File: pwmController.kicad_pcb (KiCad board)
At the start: 2 copper layers, 100 x 70 mm, 48 parts, among them J1 RJ12, J14 inputs, J16 relays, J17 relays, J5 power, J6 gnd, J7 inputs, J8 track out, K1 G5V-1, K2 G5V-1, K3 G5V-1, K4 G5V-1, K5 G5V-1, K6 G5V-1, K7 G5V-1, K8 G5V-1, U1 24LC256, U2 MAX485E, U3 L298N, U4 MCP23017_SP, U5 ULN2803A, U6 PCF8574, U7 Buck

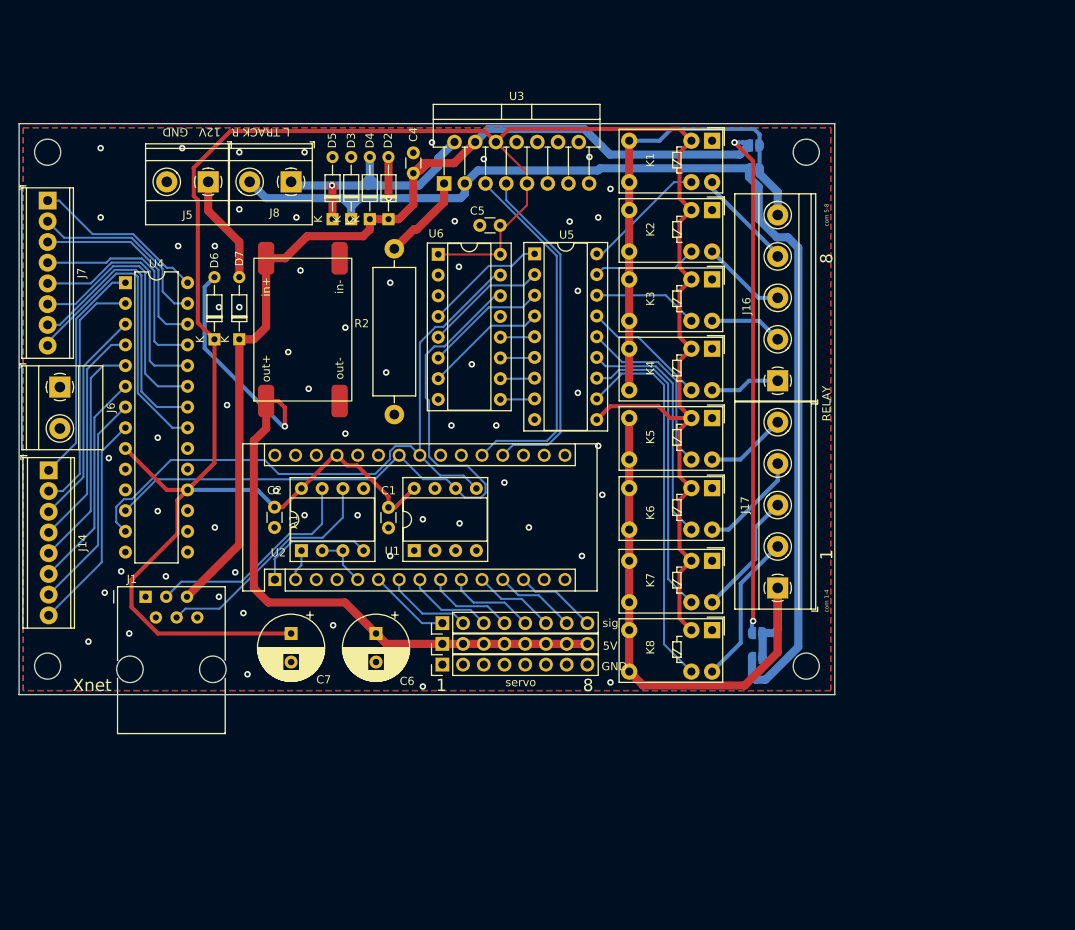
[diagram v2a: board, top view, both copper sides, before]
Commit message: made drastic changes to PCB design. I added 2nd Rj12 connector, side by side connectors, 2 analog inpouts and 2nd channel of H bridge is commissioned
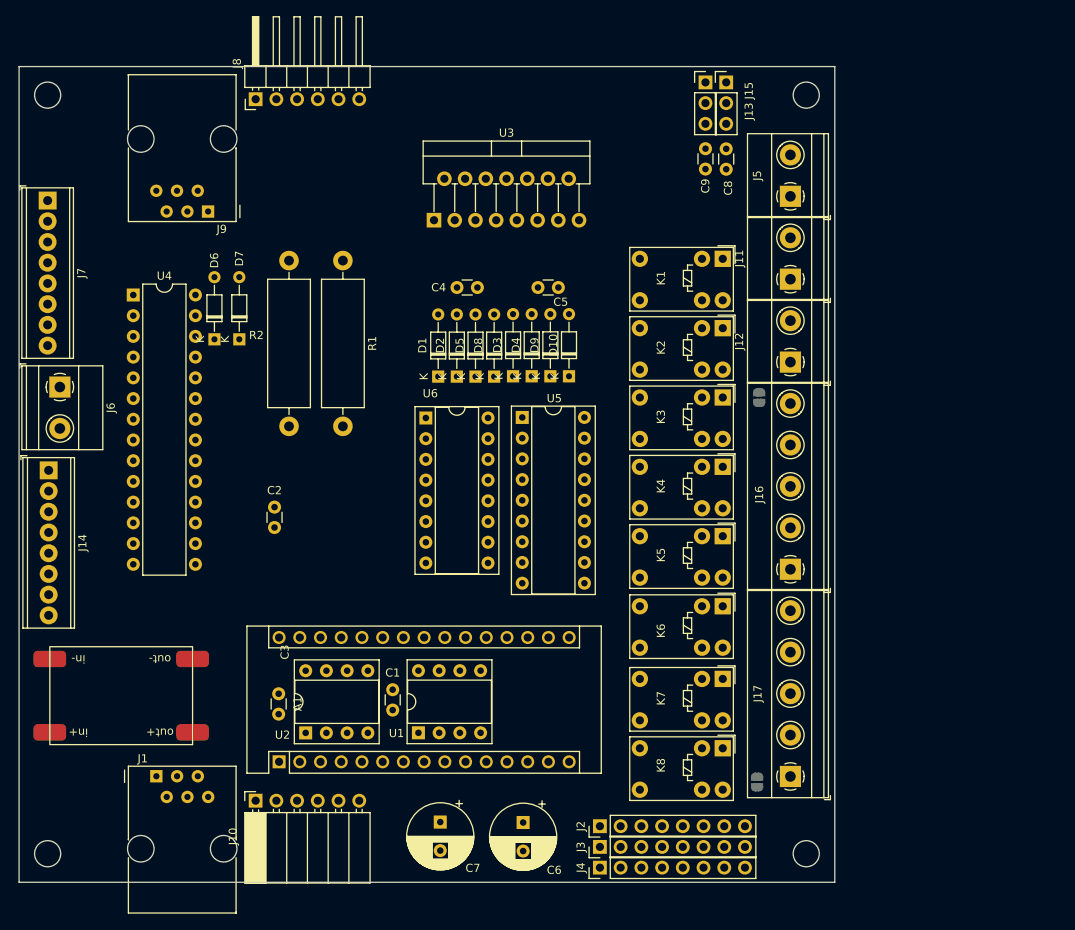
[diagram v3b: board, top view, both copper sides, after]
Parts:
- removed 5V, GND, sig: Conn_01x08_Male, Connector_PinHeader_2.54mm:PinHeader_1x08_P2.54mm_Vertical
- removed JP2, JP4: jmp, Jumper:SolderJumper-2_P1.3mm_Open_RoundedPad1.0x1.5mm
- removed the REF** at (71.5, 99.5)
- removed the REF** at (164.5, 99.5)
- removed the REF** at (164.5, 36.5)
- removed the REF** at (71.5, 36.5)
- added C3: 100nF, Capacitor_THT:C_Disc_D3.0mm_W1.6mm_P2.50mm, F.Cu at (99.8, 102.9)
- added C8: 100nF, Capacitor_THT:C_Disc_D3.0mm_W1.6mm_P2.50mm, F.Cu at (154.7, 38.6)
- added C9: 100nF, Capacitor_THT:C_Disc_D3.0mm_W1.6mm_P2.50mm, F.Cu at (152.1, 38.6)
- added D1: D, Diode_THT:D_DO-34_SOD68_P7.62mm_Horizontal, F.Cu at (119.4, 64.0)
- added D10: D, Diode_THT:D_DO-34_SOD68_P7.62mm_Horizontal, F.Cu at (135.4, 64.0)
- added D8: D, Diode_THT:D_DO-34_SOD68_P7.62mm_Horizontal, F.Cu at (126.2, 64.0)
- added D9: D, Diode_THT:D_DO-34_SOD68_P7.62mm_Horizontal, F.Cu at (133.1, 64.0)
- added J10: Conn_01x06_Female, Connector_PinSocket_2.54mm:PinSocket_1x06_P2.54mm_Horizontal, F.Cu at (97.0, 116.0)
- added J11: track out, TerminalBlock_Phoenix:TerminalBlock_Phoenix_MKDS-1,5-2-5.08_1x02_P5.08mm_Horizontal, F.Cu at (162.6, 52.1)
- added J12: track out, TerminalBlock_Phoenix:TerminalBlock_Phoenix_MKDS-1,5-2-5.08_1x02_P5.08mm_Horizontal, F.Cu at (162.6, 62.2)
- added J13: ADC, Connector_PinHeader_2.54mm:PinHeader_1x03_P2.54mm_Vertical, F.Cu at (152.1, 27.9)
- added J15: ADC, Connector_PinHeader_2.54mm:PinHeader_1x03_P2.54mm_Vertical, F.Cu at (154.7, 27.9)
- added J2: Conn_01x08_Male, Connector_PinHeader_2.54mm:PinHeader_1x08_P2.54mm_Vertical, F.Cu at (139.2, 119.1)
- added J3: Conn_01x08_Male, Connector_PinHeader_2.54mm:PinHeader_1x08_P2.54mm_Vertical, F.Cu at (139.2, 121.7)
- added J4: Conn_01x08_Male, Connector_PinHeader_2.54mm:PinHeader_1x08_P2.54mm_Vertical, F.Cu at (139.2, 124.2)
- added J9: RJ12, Connector_RJ:RJ12_Amphenol_54601, F.Cu at (91.2, 43.8)
- added R1: R, Resistor_THT:R_Axial_DIN0516_L15.5mm_D5.0mm_P20.32mm_Horizontal, F.Cu at (107.7, 49.8)
- added REF**: MountingHole_3.2mm_M3, MountingHole:MountingHole_3.2mm_M3, F.Cu at (164.5, 29.5)
- added REF**: MountingHole_3.2mm_M3, MountingHole:MountingHole_3.2mm_M3, F.Cu at (164.5, 122.5)
- added REF**: MountingHole_3.2mm_M3, MountingHole:MountingHole_3.2mm_M3, F.Cu at (71.5, 122.5)
- added REF**: MountingHole_3.2mm_M3, MountingHole:MountingHole_3.2mm_M3, F.Cu at (71.5, 29.5)
- J8: value track out -> Conn_01x06_Male; footprint TerminalBlock_Phoenix:TerminalBlock_Phoenix_MKDS-1,5-2-5.08_1x02_P5.08mm_Horizontal -> Connector_PinHeader_2.54mm:PinHeader_1x06_P2.54mm_Horizontal
- moved J5 71.4 mm to (162.6, 41.9), turned to 90 degrees
- moved U7 47.9 mm to (82.8, 104.6), turned to 180 degrees
- moved JP1 30.9 mm to (158.7, 66.6), turned to -90 degrees
- moved C7 29.5 mm to (119.6, 118.6)
- moved C6 29.4 mm to (129.8, 118.7)
- moved D3 27.7 mm to (128.6, 64.0)
- moved D4 27.7 mm to (130.8, 64.0)
- moved D5 26.1 mm to (124.0, 64.0)
- moved J17 23.2 mm to (162.6, 113.0)
- moved J16 23.2 mm to (162.6, 87.6)
- moved U2 22.3 mm to (103.1, 107.7)
- moved A1 22.3 mm to (99.9, 111.2)
- moved C1 22.3 mm to (113.8, 102.4)
- moved U1 22.3 mm to (117.0, 107.7)
- moved J1 22.0 mm to (84.8, 113.0)
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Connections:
- net /coil5_ renamed Net-(U6-Pad7)
- net /coil6_ renamed Net-(U6-Pad6)
- net /coil7_ renamed Net-(U6-Pad5)
- net /coil8_ renamed Net-(U6-Pad4)
- A1 pad 12: servo7 -> pwm2
- A1 pad 13: servo8 -> pwm1
- A1 pad 14: unconnected-(A1-Pad14) -> pwm3
- A1 pad 15: unconnected-(A1-Pad15) -> pwm4
- A1 pad 19: pwm1 -> servo7
- A1 pad 20: pwm2 -> servo8
- A1 pad 21: overcurrent -> ADC1
- A1 pad 22: unconnected-(A1-Pad22) -> ADC2
- A1 pad 25: unconnected-(A1-Pad25) -> CS1
- A1 pad 26: unconnected-(A1-Pad26) -> CS2
- D2 pad 1: +12V -> track1R
- D2 pad 2: /rightTrack -> GND
- D3 pad 1: /rightTrack -> +12V
- D3 pad 2: GND -> track2R
- D4 pad 1: +12V -> track2R
- D4 pad 2: Net-(D4-Pad2) -> GND
- D5 pad 1: Net-(D4-Pad2) -> +12V
- D5 pad 2: GND -> track1L
- D7 pad 1: +12V -> Net-(U7-Pad4)
- J1 pad 3: Net-(J1-Pad3) -> /B
- J1 pad 4: Net-(J1-Pad4) -> /A
- J8 pad 1: Net-(D4-Pad2) -> GND
- J8 pad 2: /rightTrack -> GND
- R2 pad 1: Net-(R2-Pad1) -> GND
- R2 pad 2: GND -> CS1
- U2 pad 6: Net-(J1-Pad4) -> /A
- U2 pad 7: Net-(J1-Pad3) -> /B
- U3 pad 1: Net-(R2-Pad1) -> CS1
- U3 pad 10: unconnected-(U3-Pad10) -> pwm4
- U3 pad 11: unconnected-(U3-Pad11) -> +5V
- U3 pad 12: unconnected-(U3-Pad12) -> pwm3
- U3 pad 13: unconnected-(U3-Pad13) -> track2R
- U3 pad 14: unconnected-(U3-Pad14) -> track2L
- U3 pad 15: unconnected-(U3-Pad15) -> CS2
- U3 pad 2: Net-(D4-Pad2) -> track1R
- U3 pad 3: /rightTrack -> track1L
- U5 pad 5: /coil4_ -> Net-(U6-Pad9)
- U5 pad 6: /coil3_ -> Net-(U6-Pad10)
- U5 pad 7: /coil2_ -> Net-(U6-Pad11)
- U5 pad 8: /coil1_ -> Net-(U6-Pad12)
- U6 pad 10: /coil2_ -> Net-(U6-Pad10)
- U6 pad 11: /coil3_ -> Net-(U6-Pad11)
- U6 pad 12: /coil4_ -> Net-(U6-Pad12)
- U6 pad 9: /coil1_ -> Net-(U6-Pad9)
- U7 pad 4: +12V -> Net-(U7-Pad4)
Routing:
- net +5V: track 296.2 -> 0.00 mm
- net +12V: track 183.0 -> 0.00 mm, vias 2 -> 0
- net /rightTrack: track 146.5 -> 0.00 mm, vias 1 -> 0
- net +5VA: track 95.2 -> 0.00 mm, vias 1 -> 0
- net SCL: track 83.5 -> 0.00 mm
- net SDA: track 81.9 -> 0.00 mm
- net Net-(J17-Pad1): track 69.8 -> 0.00 mm
- net Net-(J16-Pad5): track 58.2 -> 0.00 mm
- net /coil8: track 46.8 -> 0.00 mm
- net pwm2: track 44.4 -> 0.00 mm
- net pwm1: track 41.5 -> 0.00 mm
- net /coil7: track 37.8 -> 0.00 mm
- net Net-(J7-Pad8): track 37.3 -> 0.00 mm
- net Net-(J7-Pad7): track 35.3 -> 0.00 mm
- net Net-(D4-Pad2): track 33.7 -> 0.00 mm, vias 1 -> 0
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- removed copper zone on B.Cu, net GND
- removed copper zone on F.Cu, net GND
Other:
- board size 100 x 70 mm -> 100 x 100 mm
- board text removed: "1"
- board text removed: "12V"
- board text removed: "8"
- board text removed: "L TRACK R 12V GND"
- board text removed: "RELAY"
- board text removed: "Xnet"
- board text removed: "Xnet PWM controller And IO module V1.0 By Bas Knippels"
- board text removed: "com 1-4"
- board text removed: "com 5-8"
- board text removed: "servo"
- board text removed: "track right"

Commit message: divided the schematic in several sheets.
PCB needs to be redrawn because the link between components is gone
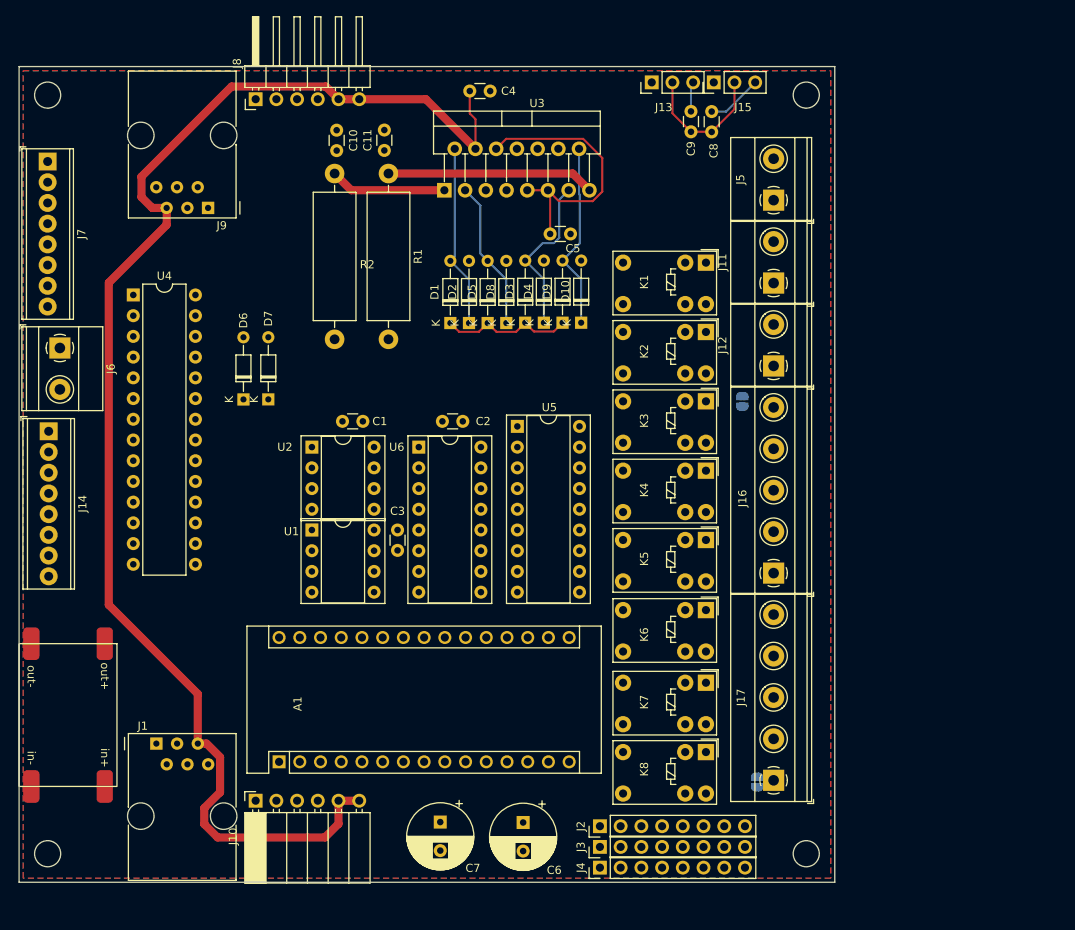
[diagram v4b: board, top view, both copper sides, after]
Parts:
- added C10: 100nF, Capacitor_THT:C_Disc_D3.0mm_W1.6mm_P2.50mm, F.Cu at (106.9, 33.8)
- added C11: 100nF, Capacitor_THT:C_Disc_D3.0mm_W1.6mm_P2.50mm, F.Cu at (112.8, 36.3)
- moved U2 35.0 mm to (103.9, 72.7), turned to 0 degrees
- moved C1 33.1 mm to (110.1, 69.5), turned to 180 degrees
- moved U1 28.1 mm to (103.9, 82.8), turned to 0 degrees
- moved C2 25.4 mm to (122.4, 69.5), turned to 180 degrees
- moved C3 24.8 mm to (114.4, 82.8)
- moved C4 24.1 mm to (123.2, 29.0), turned to 0 degrees
- moved R1 12.0 mm to (113.3, 39.1)
- moved R2 11.2 mm to (106.7, 59.4), turned to 90 degrees
- moved D7 8.18 mm to (98.6, 66.8)
- moved D6 8.18 mm to (95.5, 66.8)
- moved U7 7.40 mm to (75.5, 103.2), turned to -90 degrees
- moved C5 6.73 mm to (133.1, 46.5)
- moved D1 6.73 mm to (120.9, 57.4)
- moved D10 6.73 mm to (136.9, 57.4)
- moved D2 6.73 mm to (123.2, 57.4)
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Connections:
- U5 pad 5: Net-(U6-Pad9) -> Net-(U5-Pad5)
- U5 pad 6: Net-(U6-Pad10) -> Net-(U5-Pad6)
- U5 pad 7: Net-(U6-Pad11) -> Net-(U5-Pad7)
- U5 pad 8: Net-(U6-Pad12) -> Net-(U5-Pad8)
- U6 pad 10: Net-(U6-Pad10) -> Net-(U5-Pad7)
- U6 pad 11: Net-(U6-Pad11) -> Net-(U5-Pad6)
- U6 pad 12: Net-(U6-Pad12) -> Net-(U5-Pad5)
- U6 pad 9: Net-(U6-Pad9) -> Net-(U5-Pad8)
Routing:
- net +12V: track 0.00 -> 187.4 mm
- net +5V: track 0.00 -> 51.1 mm
- net CS2: track 0.00 -> 25.5 mm
- net track2L: track 0.00 -> 23.2 mm
- net track1R: track 0.00 -> 22.5 mm
- net track2R: track 0.00 -> 20.2 mm
- net track1L: track 0.00 -> 18.4 mm
- net CS1: track 0.00 -> 14.3 mm
- net ADC1: track 0.00 -> 6.82 mm
- net ADC2: track 0.00 -> 3.67 mm
- added copper zone on B.Cu, net GND
- added copper zone on F.Cu, net GND

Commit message: changed PCB layout. I want to change more
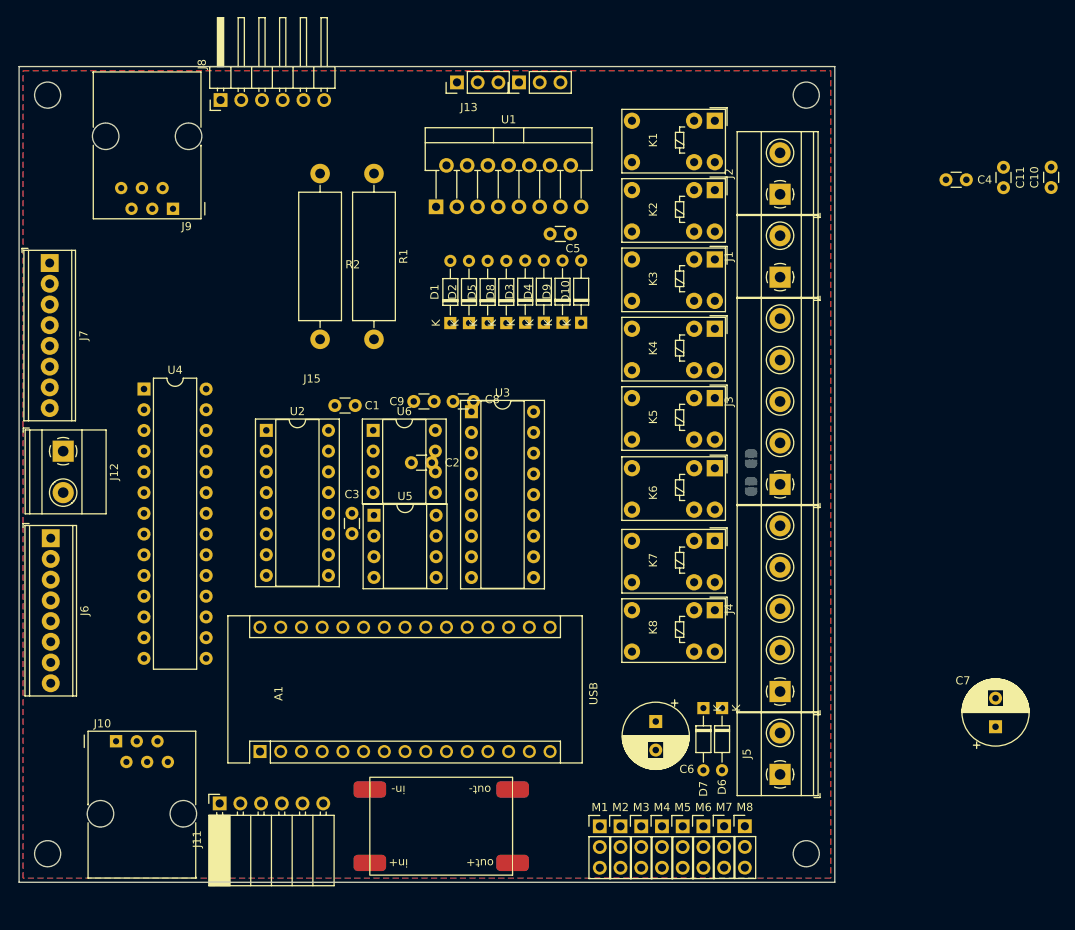
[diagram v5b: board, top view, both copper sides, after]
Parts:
- removed J14: inputs, TerminalBlock_Phoenix:TerminalBlock_Phoenix_MPT-0,5-8-2.54_1x08_P2.54mm_Horizontal
- removed J16, J17: relays, TerminalBlock_Phoenix:TerminalBlock_Phoenix_MKDS-1,5-5-5.08_1x05_P5.08mm_Horizontal
- removed JP3: jmp, Jumper:SolderJumper-2_P1.3mm_Open_RoundedPad1.0x1.5mm
- added JP2: jmp, Jumper:SolderJumper-2_P1.3mm_Open_RoundedPad1.0x1.5mm, B.Cu at (157.7, 77.5)
- added M1: Motor_Servo, Connector_PinHeader_2.54mm:PinHeader_1x03_P2.54mm_Vertical, F.Cu at (139.2, 119.1)
- added M2: Motor_Servo, Connector_PinHeader_2.54mm:PinHeader_1x03_P2.54mm_Vertical, F.Cu at (141.7, 119.1)
- added M3: Motor_Servo, Connector_PinHeader_2.54mm:PinHeader_1x03_P2.54mm_Vertical, F.Cu at (144.3, 119.1)
- added M4: Motor_Servo, Connector_PinHeader_2.54mm:PinHeader_1x03_P2.54mm_Vertical, F.Cu at (146.8, 119.1)
- added M5: Motor_Servo, Connector_PinHeader_2.54mm:PinHeader_1x03_P2.54mm_Vertical, F.Cu at (149.4, 119.1)
- added M6: Motor_Servo, Connector_PinHeader_2.54mm:PinHeader_1x03_P2.54mm_Vertical, F.Cu at (151.9, 119.1)
- added M7: Motor_Servo, Connector_PinHeader_2.54mm:PinHeader_1x03_P2.54mm_Vertical, F.Cu at (154.4, 119.1)
- added M8: Motor_Servo, Connector_PinHeader_2.54mm:PinHeader_1x03_P2.54mm_Vertical, F.Cu at (157.0, 119.1)
- J1: value RJ12 -> track out; footprint Connector_RJ:RJ12_Amphenol_54601 -> TerminalBlock_Phoenix:TerminalBlock_Phoenix_MKDS-1,5-2-5.08_1x02_P5.08mm_Horizontal
- J10: value Conn_01x06_Female -> RJ12; footprint Connector_PinSocket_2.54mm:PinSocket_1x06_P2.54mm_Horizontal -> Connector_RJ:RJ12_Amphenol_54601
- J11: value track out -> Conn_01x06_Female; footprint TerminalBlock_Phoenix:TerminalBlock_Phoenix_MKDS-1,5-2-5.08_1x02_P5.08mm_Horizontal -> Connector_PinSocket_2.54mm:PinSocket_1x06_P2.54mm_Horizontal
- J12: value track out -> gnd
- J2: value Conn_01x08_Male -> track out; footprint Connector_PinHeader_2.54mm:PinHeader_1x08_P2.54mm_Vertical -> TerminalBlock_Phoenix:TerminalBlock_Phoenix_MKDS-1,5-2-5.08_1x02_P5.08mm_Horizontal
- J3, J4: value Conn_01x08_Male -> relays; footprint Connector_PinHeader_2.54mm:PinHeader_1x08_P2.54mm_Vertical -> TerminalBlock_Phoenix:TerminalBlock_Phoenix_MKDS-1,5-5-5.08_1x05_P5.08mm_Horizontal
- J6: value gnd -> inputs; footprint TerminalBlock_Phoenix:TerminalBlock_Phoenix_MKDS-1,5-2-5.08_1x02_P5.08mm_Horizontal -> TerminalBlock_Phoenix:TerminalBlock_Phoenix_MPT-0,5-8-2.54_1x08_P2.54mm_Horizontal
- U1: value 24LC256 -> L298N; footprint Package_DIP:DIP-8_W7.62mm_Socket -> Package_TO_SOT_THT:TO-220-15_P2.54x2.54mm_StaggerOdd_Lead4.58mm_Vertical
- U2: value MAX485E -> PCF8574; footprint Package_DIP:DIP-8_W7.62mm_Socket -> Package_DIP:DIP-16_W7.62mm_Socket
- U3: value L298N -> ULN2803A; footprint Package_TO_SOT_THT:TO-220-15_P2.54x2.54mm_StaggerOdd_Lead4.58mm_Vertical -> Package_DIP:DIP-18_W7.62mm_Socket
- U5: value ULN2803A -> MAX485E; footprint Package_DIP:DIP-18_W7.62mm_Socket -> Package_DIP:DIP-8_W7.62mm_Socket
- U6: value PCF8574 -> 24LC256; footprint Package_DIP:DIP-16_W7.62mm_Socket -> Package_DIP:DIP-8_W7.62mm_Socket
- moved J1 95.5 mm to (161.3, 51.8), turned to 90 degrees
- moved J11 93.2 mm to (92.6, 116.3)
- moved C10 87.9 mm to (194.5, 40.8), turned to 90 degrees
- moved J12 87.7 mm to (73.4, 73.2), turned to -90 degrees
- moved J2 80.6 mm to (161.3, 41.7)
- moved C11 75.9 mm to (188.7, 38.4), turned to -90 degrees
- moved J5 70.4 mm to (161.3, 112.8)
- moved D6 69.8 mm to (154.2, 104.6), turned to -90 degrees
- moved C7 69.1 mm to (187.7, 106.9), turned to 90 degrees
- moved D7 65.4 mm to (151.9, 104.6), turned to -90 degrees
- moved C4 59.4 mm to (181.6, 39.9)
- moved U7 49.6 mm to (122.0, 120.6), turned to 180 degrees
- moved J3 49.6 mm to (161.3, 77.2)
- moved C9 47.4 mm to (116.4, 67.1), turned to 0 degrees
- moved C8 44.1 mm to (123.7, 67.1), turned to 180 degrees
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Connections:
- A1 pad 12: pwm2 -> pwm1
- A1 pad 13: pwm1 -> pwm2
- C1 pad 1: +5V -> GND
- C1 pad 2: GND -> CS1
- C10 pad 1: GND -> +5V
- C10 pad 2: CS1 -> ADC1
- C11 pad 1: CS2 -> +5V
- C11 pad 2: GND -> ADC2
- C3 pad 1: +5V -> CS2
- C8 pad 2: ADC1 -> GND
- C9 pad 2: ADC2 -> GND
- D6 pad 1: +5V -> Net-(U7-Pad4)
- D6 pad 2: +5VA -> Net-(J5-Pad1)
- D7 pad 1: Net-(D7-Pad1) -> +5V
- D7 pad 2: Net-(D7-Pad2) -> +5VA
- J1 pad 1: unconnected-(J1-Pad1) -> track1L
- J1 pad 2: GND -> track1R
- J10 pad 1: GND -> unconnected-(J10-Pad1)
- J10 pad 3: /B -> /interface/B
- J10 pad 4: /A -> /interface/A
- J10 pad 6: +12V -> unconnected-(J10-Pad6)
- J11 pad 1: track1L -> GND
- J11 pad 2: track1R -> GND
- J12 pad 1: track2L -> GND
- J12 pad 2: track2R -> GND
- J2 pad 1: servo1 -> track2L
- J2 pad 2: servo2 -> track2R
- J3 pad 1: +5VA -> Net-(K4-Pad10)
- J3 pad 2: +5VA -> Net-(K3-Pad10)
- J3 pad 3: +5VA -> Net-(K2-Pad10)
- J3 pad 4: +5VA -> Net-(K1-Pad10)
- J3 pad 5: +5VA -> Net-(JP1-Pad2)
- J4 pad 1: GND -> Net-(JP2-Pad2)
- J4 pad 2: GND -> Net-(J4-Pad2)
- J4 pad 3: GND -> Net-(J4-Pad3)
- J4 pad 4: GND -> Net-(J4-Pad4)
- J4 pad 5: GND -> Net-(J4-Pad5)
- J5 pad 1: Net-(D7-Pad2) -> Net-(J5-Pad1)
- J6 pad 1: GND -> Net-(J6-Pad1)
- J6 pad 2: GND -> Net-(J6-Pad2)
- J8 pad 3: /B -> /interface/B
- J8 pad 4: /A -> /interface/A
- J9 pad 3: /B -> /interface/B
- J9 pad 4: /A -> /interface/A
- JP1 pad 2: Net-(J16-Pad5) -> Net-(JP1-Pad2)
- K1 pad 10: Net-(J16-Pad4) -> Net-(K1-Pad10)
- K1 pad 5: Net-(J16-Pad5) -> Net-(JP1-Pad2)
- K1 pad 6: Net-(J16-Pad5) -> Net-(JP1-Pad2)
- K1 pad 9: /coil1 -> /relays/coil5
- K2 pad 10: Net-(J16-Pad3) -> Net-(K2-Pad10)
- K2 pad 5: Net-(J16-Pad5) -> Net-(JP1-Pad2)
- K2 pad 6: Net-(J16-Pad5) -> Net-(JP1-Pad2)
- K2 pad 9: /coil2 -> /relays/coil6
- K3 pad 10: Net-(J16-Pad2) -> Net-(K3-Pad10)
- K3 pad 5: Net-(J16-Pad5) -> Net-(JP1-Pad2)
- K3 pad 6: Net-(J16-Pad5) -> Net-(JP1-Pad2)
- K3 pad 9: /coil3 -> /relays/coil7
- K4 pad 10: Net-(J16-Pad1) -> Net-(K4-Pad10)
- K4 pad 5: Net-(J16-Pad5) -> Net-(JP1-Pad2)
- K4 pad 6: Net-(J16-Pad5) -> Net-(JP1-Pad2)
- K4 pad 9: /coil4 -> /relays/coil8
- K5 pad 10: Net-(J17-Pad5) -> Net-(J4-Pad5)
- K5 pad 5: Net-(J17-Pad1) -> Net-(JP2-Pad2)
- K5 pad 6: Net-(J17-Pad1) -> Net-(JP2-Pad2)
- K5 pad 9: /coil5 -> /relays/coil1
- K6 pad 10: Net-(J17-Pad4) -> Net-(J4-Pad4)
- K6 pad 5: Net-(J17-Pad1) -> Net-(JP2-Pad2)
- K6 pad 6: Net-(J17-Pad1) -> Net-(JP2-Pad2)
- K6 pad 9: /coil6 -> /relays/coil2
- K7 pad 10: Net-(J17-Pad3) -> Net-(J4-Pad3)
- K7 pad 5: Net-(J17-Pad1) -> Net-(JP2-Pad2)
- K7 pad 6: Net-(J17-Pad1) -> Net-(JP2-Pad2)
- K7 pad 9: /coil7 -> /relays/coil3
- K8 pad 10: Net-(J17-Pad2) -> Net-(J4-Pad2)
- K8 pad 5: Net-(J17-Pad1) -> Net-(JP2-Pad2)
- K8 pad 6: Net-(J17-Pad1) -> Net-(JP2-Pad2)
- K8 pad 9: /coil8 -> /relays/coil4
- R1 pad 1: CS2 -> GND
- R1 pad 2: GND -> CS1
- R2 pad 1: GND -> CS2
- R2 pad 2: CS1 -> GND
- U1 pad 1: GND -> CS1
- U1 pad 2: GND -> track1R
- U1 pad 3: GND -> track1L
- U1 pad 4: GND -> +12V
- U1 pad 5: SDA -> pwm2
- U1 pad 6: SCL -> +5V
- U1 pad 7: GND -> pwm1
- U1 pad 8: +5V -> GND
- U2 pad 1: Rx -> +5V
- U2 pad 2: 485dir -> GND
- U2 pad 3: 485dir -> GND
- U2 pad 4: Tx -> Net-(U2-Pad4)
- U2 pad 5: GND -> Net-(U2-Pad5)
- U2 pad 6: /A -> Net-(U2-Pad6)
- U2 pad 7: /B -> Net-(U2-Pad7)
- U2 pad 8: +5V -> GND
- U3 pad 1: CS1 -> Net-(U2-Pad4)
- U3 pad 10: pwm4 -> +5V
- U3 pad 11: +5V -> /relays/coil8
- U3 pad 12: pwm3 -> /relays/coil7
- U3 pad 13: track2R -> /relays/coil6
- U3 pad 14: track2L -> /relays/coil5
- U3 pad 15: CS2 -> /relays/coil4
- U3 pad 2: track1R -> Net-(U2-Pad5)
- U3 pad 3: track1L -> Net-(U2-Pad6)
- U3 pad 4: +12V -> Net-(U2-Pad7)
- U3 pad 5: pwm2 -> Net-(U2-Pad12)
- U3 pad 6: +5V -> Net-(U2-Pad11)
- U3 pad 7: pwm1 -> Net-(U2-Pad10)
- U3 pad 8: GND -> Net-(U2-Pad9)
- U3 pad 9: +5V -> GND
- U4 pad 1: Net-(J14-Pad1) -> Net-(J6-Pad1)
- U4 pad 2: Net-(J14-Pad2) -> Net-(J6-Pad2)
- U4 pad 3: Net-(J14-Pad3) -> Net-(J6-Pad3)
- U4 pad 4: Net-(J14-Pad4) -> Net-(J6-Pad4)
- U4 pad 5: Net-(J14-Pad5) -> Net-(J6-Pad5)
- U4 pad 6: Net-(J14-Pad6) -> Net-(J6-Pad6)
- U4 pad 7: Net-(J14-Pad7) -> Net-(J6-Pad7)
- U4 pad 8: Net-(J14-Pad8) -> Net-(J6-Pad8)
- U5 pad 1: Net-(U5-Pad1) -> Rx
- U5 pad 2: Net-(U5-Pad2) -> 485dir
- U5 pad 3: Net-(U5-Pad3) -> 485dir
- U5 pad 4: Net-(U5-Pad4) -> Tx
- U5 pad 5: Net-(U5-Pad5) -> GND
- U5 pad 6: Net-(U5-Pad6) -> /interface/A
- U5 pad 7: Net-(U5-Pad7) -> /interface/B
- U5 pad 8: Net-(U5-Pad8) -> +5V
- U6 pad 1: +5V -> GND
- U6 pad 4: Net-(U5-Pad1) -> GND
- U6 pad 5: Net-(U5-Pad2) -> SDA
- U6 pad 6: Net-(U5-Pad3) -> SCL
- U6 pad 7: Net-(U5-Pad4) -> GND
- U6 pad 8: GND -> +5V
- U7 pad 4: Net-(D7-Pad1) -> Net-(U7-Pad4)
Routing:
- net +12V: track 187.4 -> 0.00 mm
- net +5V: track 51.1 -> 0.00 mm
- net CS2: track 25.5 -> 0.00 mm
- net track2L: track 23.2 -> 0.00 mm
- net track1R: track 22.5 -> 0.00 mm
- net track2R: track 20.2 -> 0.00 mm
- net track1L: track 18.4 -> 0.00 mm
- net CS1: track 14.3 -> 0.00 mm
- net ADC1: track 6.82 -> 0.00 mm
- net ADC2: track 3.67 -> 0.00 mm
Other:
- board text added: "USB"
